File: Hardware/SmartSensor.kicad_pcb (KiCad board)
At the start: 2 copper layers, 68.8 x 68.1 mm, 72 parts, among them IC1 VEML7700-TT, IC2 SHTC3, IC3 XB24CZ7PIT-004, IC4 ATECC608B-SSHDA-B, J1 USB_B_Micro, J10 PANTS_1, J11 PANTS_3, J12 PANTS_4, J2 BAT_1, J3 BAT_2, J4 Conn_01x06_Male, J5 Conn_02x05_Odd_Even, J6 Conn_02x05_Odd_Even, J7 Conn_01x02_Male, J8 Conn_01x06_Male, J9 Conn_02x04_Odd_Even, Q1 DMG2301L, Q2 DMG2301L, Q3 DMG2301L, Q4 DMG2301L, Q5 DMG2301L, SW1 RESET, SW2 COMMISSIONING, U1 TPS63001, U2 CCS811, U3 MCP7940N-xSN, U4 ATmega324PB-AU, Y1 20MHz, Y2 Crystal

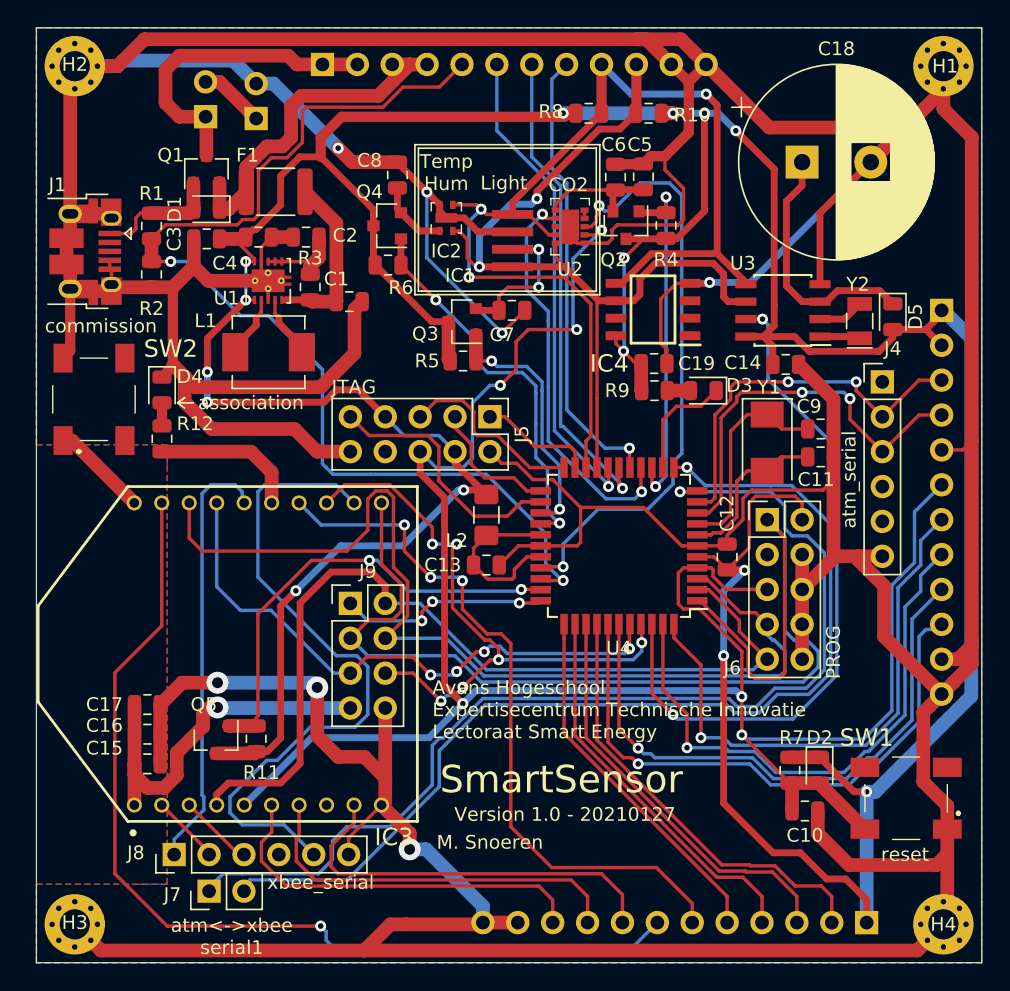
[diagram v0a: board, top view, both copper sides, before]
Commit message: Modified hardware and fixed errors found in v1.0
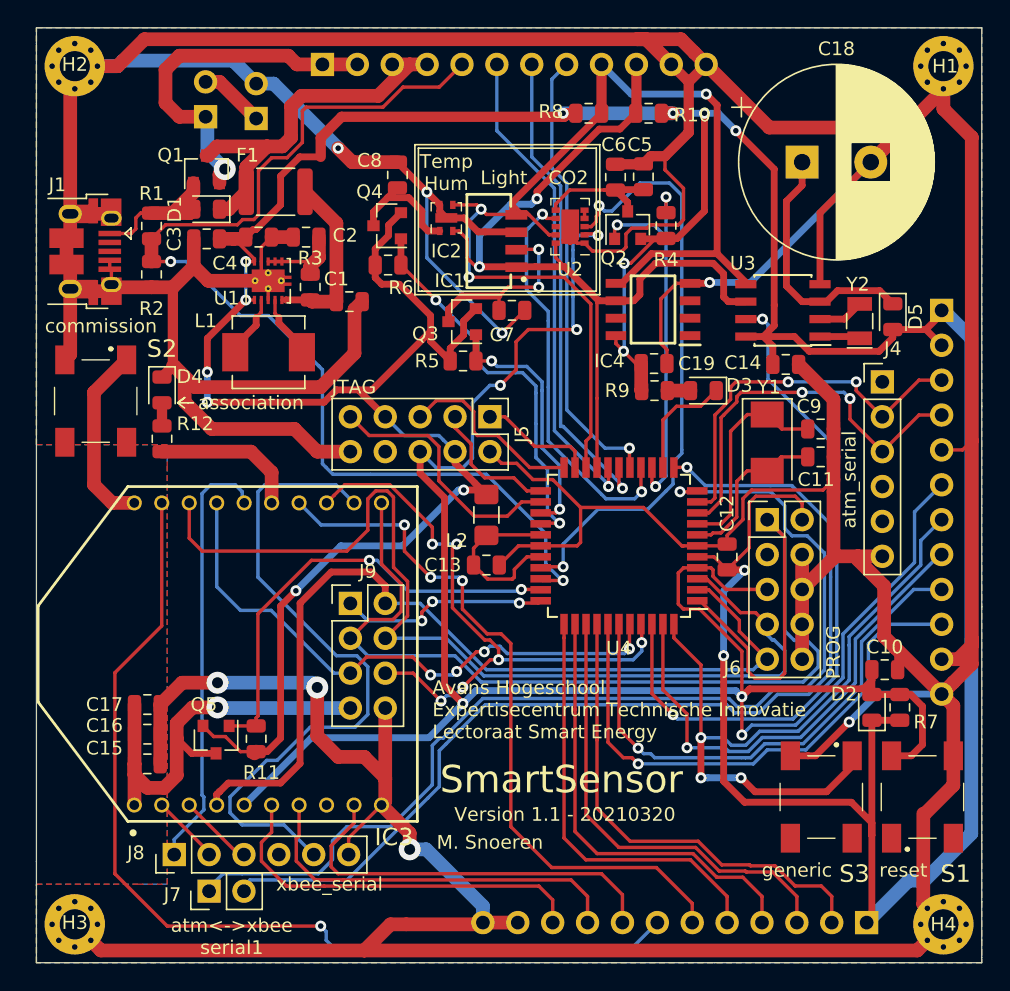
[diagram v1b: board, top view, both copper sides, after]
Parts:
- removed SW1: RESET, LL3301AF065QJ:LL3301FF065QJ
- removed SW2: COMMISSIONING, LL3301AF065QJ:LL3301FF065QJ
- added S1: LL3301FF065QJ, SamacSys_Parts:LL3301FF065QJ, F.Cu at (228.0, 134.6)
- added S2: LL3301FF065QJ, SamacSys_Parts:LL3301FF065QJ, F.Cu at (167.8, 105.8)
- added S3: LL3301FF065QJ, SamacSys_Parts:LL3301FF065QJ, F.Cu at (220.6, 134.6)
- IC1: footprint SmartSensor:VEML7700 -> SamacSys_Parts:VEML7700
- moved C10 11.8 mm to (225.2, 125.3)
- moved R7 9.22 mm to (226.3, 128.1), turned to 90 degrees
- moved D2 5.95 mm to (224.3, 128.1), turned to 90 degrees
- moved IC1 3.47 mm to (198.0, 97.5), turned to 90 degrees
- moved Q2 0.13 mm to (206.5, 93.0), turned to 90 degrees
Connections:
- Q1 pad 2: V_IN -> /Interface/V_BAT
- Q1 pad 3: /Interface/V_BAT -> V_IN
- Q2 pad 2: Net-(C5-Pad1) -> +3V3
- Q2 pad 3: +3V3 -> Net-(C5-Pad1)
- Q3 pad 2: Net-(C7-Pad1) -> +3V3
- Q3 pad 3: +3V3 -> Net-(C7-Pad1)
- Q4 pad 2: Net-(C8-Pad1) -> +3V3
- Q4 pad 3: +3V3 -> Net-(C8-Pad1)
- Q5 pad 2: Net-(C15-Pad1) -> +3V3
- Q5 pad 3: +3V3 -> Net-(C15-Pad1)
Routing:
- net +3V3: track 305.5 -> 322.6 mm, vias 15 -> 14
- net /Interface/ATM_PB4: track 40.0 -> 52.4 mm, vias 1 -> 3
- net Net-(IC3-Pad20): track 7.07 -> 13.6 mm
- net /Interface/ATM_PB3: track 41.0 -> 36.3 mm
- net GND: track 581.3 -> 585.8 mm, vias 7 -> 8
- net /Interface/ATM_PA3: track 26.7 -> 31.1 mm
- net /Interface/ATM_PA2: track 28.5 -> 32.6 mm
- net Net-(C15-Pad1): track 28.2 -> 32.2 mm
- net /Interface/ATM_SCL_1: track 42.6 -> 38.9 mm
- net Net-(C8-Pad1): track 5.29 -> 8.88 mm
- net ATM_RESET: track 154.5 -> 158.0 mm
- net Net-(C7-Pad1): track 10.6 -> 14.0 mm
- net /Interface/ATM_PA1: track 30.3 -> 33.6 mm
- net CO2_ENABLE: track 26.0 -> 29.3 mm, vias 2 -> 3
- net /Interface/ATM_SDA_1: track 42.7 -> 39.6 mm
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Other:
- board text added: "Version 1.1 - 20210320"
- board text added: "generic"
- board text removed: "Version 1.0 - 20210127"

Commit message: Added final version 1.2 to the repository
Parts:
- removed Q2, Q3, Q4, Q5: DMG2301L, Package_TO_SOT_SMD:SOT-23
- removed R11, R6: 100k, Resistor_SMD:R_0805_2012Metric
- added D6: GREEN, LED_SMD:LED_0805_2012Metric, F.Cu at (212.0, 105.0)
- R4: value 100k -> 210
- moved R5 20.1 mm to (214.6, 103.0)
- moved R4 12.0 mm to (208.4, 105.0), turned to 180 degrees
- moved C15 7.81 mm to (179.0, 129.8)
- moved C16 7.77 mm to (179.0, 127.8)
- moved C17 7.74 mm to (179.0, 125.7)
- moved R9 1.97 mm to (208.4, 107.0)
- moved D3 1.97 mm to (212.0, 107.0)
- moved C14 0.13 mm to (218.0, 103.0)
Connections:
- C15 pad 1: Net-(C15-Pad1) -> +3V3
- C16 pad 1: Net-(C15-Pad1) -> +3V3
- C17 pad 1: Net-(C15-Pad1) -> +3V3
- C5 pad 1: Net-(C5-Pad1) -> +3V3
- C6 pad 1: Net-(C5-Pad1) -> +3V3
- C7 pad 1: Net-(C7-Pad1) -> +3V3
- C8 pad 1: Net-(C8-Pad1) -> +3V3
- IC1 pad 2: Net-(C7-Pad1) -> +3V3
- IC2 pad 1: Net-(C8-Pad1) -> +3V3
- IC3 pad 1: Net-(C15-Pad1) -> +3V3
- J9 pad 7: Net-(C15-Pad1) -> +3V3
- R4 pad 1: CO2_ENABLE -> Net-(D6-Pad2)
- R5 pad 1: LS_ENABLE -> +3V3
- R5 pad 2: +3V3 -> RTC_MFP
- U2 pad 6: Net-(C5-Pad1) -> +3V3
- U4 pad 14: CO2_ENABLE -> LED_2
- U4 pad 25: LS_ENABLE -> Net-(U4-Pad25)
- U4 pad 26: HT_ENABLE -> Net-(U4-Pad26)
- U4 pad 32: XBEE_ENABLE -> Net-(U4-Pad32)
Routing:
- net +3V3: track 322.6 -> 379.8 mm, vias 14 -> 16
- net XBEE_ENABLE: track 33.4 -> 0.00 mm, vias 2 -> 0
- net Net-(C15-Pad1): track 32.2 -> 0.00 mm, vias 1 -> 0
- net CO2_ENABLE: track 29.3 -> 0.00 mm, vias 3 -> 0
- net HT_ENABLE: track 28.4 -> 0.00 mm, vias 2 -> 0
- net LS_ENABLE: track 18.7 -> 0.00 mm, vias 2 -> 0
- net Net-(C7-Pad1): track 14.0 -> 0.00 mm, vias 2 -> 0
- net Net-(C5-Pad1): track 9.19 -> 0.00 mm
- net LED_2: track 0.00 -> 8.88 mm
- net Net-(C8-Pad1): track 8.88 -> 0.00 mm
- net GND: track 585.8 -> 579.2 mm, vias 8 -> 6
- net XBEE_UART_RTS: track 31.5 -> 38.0 mm
- net RTC_MFP: track 50.0 -> 54.3 mm
- net /Interface/ADAPTER_IN_USE: track 79.3 -> 82.3 mm
- net ATM_MISO: track 66.1 -> 68.7 mm
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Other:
- board text added: "Version 1.2 - 20210614"
- board text removed: "Version 1.1 - 20210320"
